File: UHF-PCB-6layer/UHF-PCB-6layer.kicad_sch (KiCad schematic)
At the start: 34 parts, among them IC1 MC100EL1648DG, J1 Screw_Terminal_01x07, J2 Screw_Terminal_01x04, U1 MAC-24+, U2 LTC1566-1IS8-PBF, U3 TAV1-331+, U4 MAC-24+, U5 XMSM0G3507SPT, U6 XC7A100T-CSG324_A

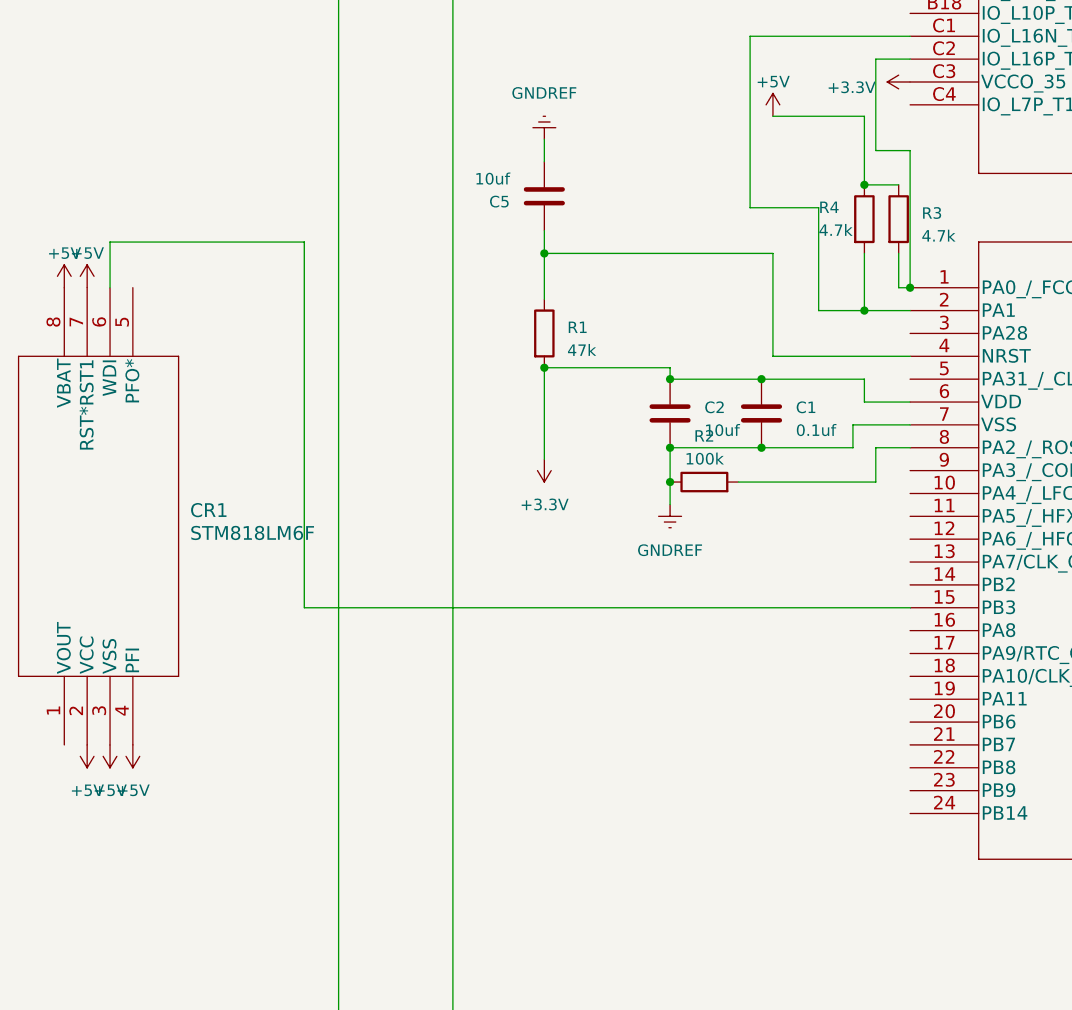
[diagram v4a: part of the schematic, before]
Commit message: draft of SVC added, needs to be vetted
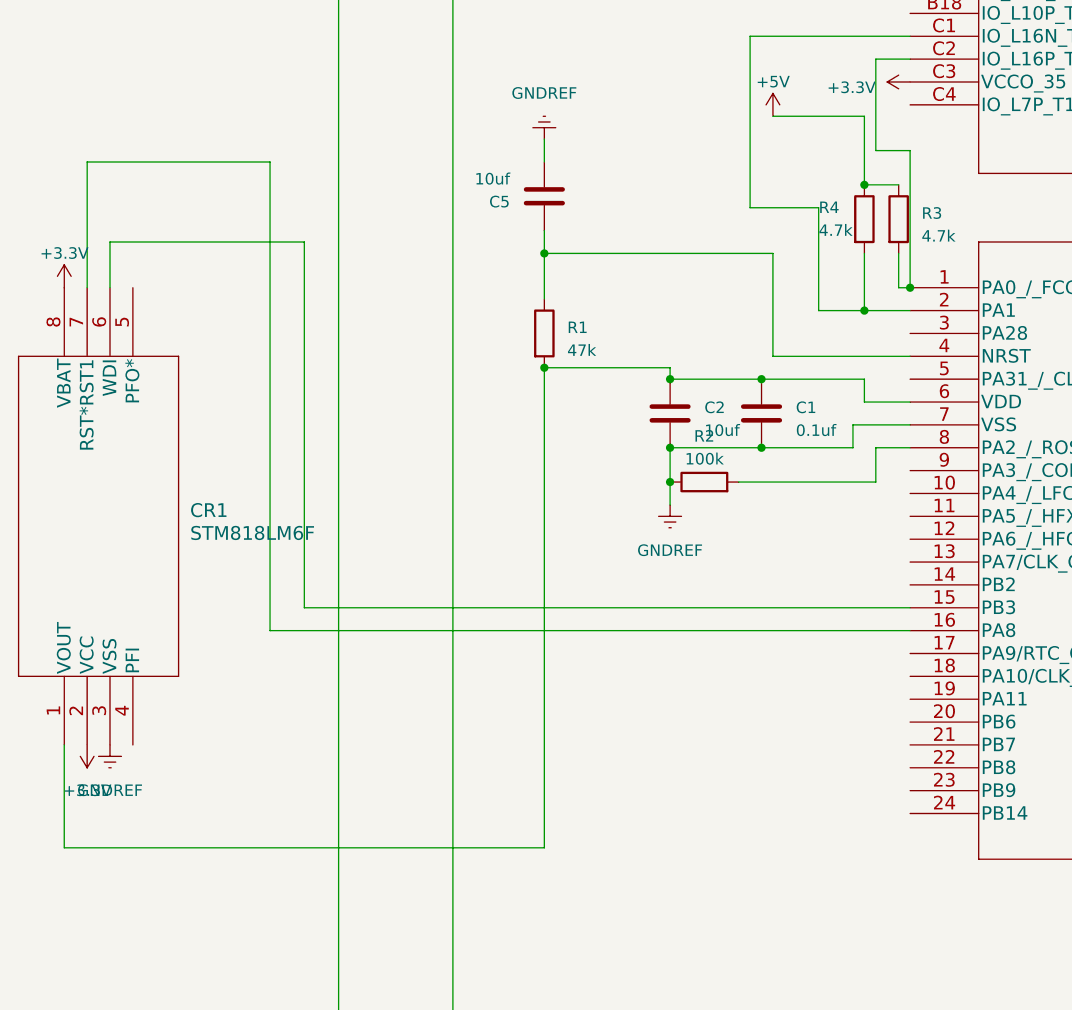
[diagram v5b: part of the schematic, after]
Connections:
- net +3.3V: now also CR1.2 (VCC), CR1.8 (VBAT); no longer C1.2, C2.2, R1.2, U5.6 (VDD)
- net +5V: no longer CR1.2 (VCC), CR1.3 (VSS), CR1.4 (PFI), CR1.7 (RST*RST1), CR1.8 (VBAT)
- net GNDREF: now also CR1.3 (VSS)
- net at CR1.1 (VOUT): now also C1.2, C2.2, R1.2, U5.6 (VDD)
- net at U5.16 (PA8): now also CR1.7 (RST*RST1)
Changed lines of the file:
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@@
+    (stroke (width 0) (type default))
+  )
+  (wire (pts (xy 57.15 209.55) (xy 128.27 209.55))
     (stroke (width 0) (type default))
   )
@@
     (stroke (width 0) (type default))
   )
+  (wire (pts (xy 87.63 233.68) (xy 34.29 233.68))
+    (stroke (width 0) (type default))
+  )
   (wire (pts (xy 295.91 222.25) (xy 290.83 222.25))
     (stroke (width 0) (type default))
@@
     (stroke (width 0) (type default))
   )
+  (wire (pts (xy 57.15 157.48) (xy 57.15 209.55))
+    (stroke (width 0) (type default))
+  )
+  (wire (pts (xy 36.83 171.45) (xy 36.83 157.48))
+    (stroke (width 0) (type default))
+  )
   (wire (pts (xy 267.97 190.5) (xy 267.97 194.31))
     (stroke (width 0) (type default))
@@
     (stroke (width 0) (type default))
   )
+  (wire (pts (xy 36.83 157.48) (xy 57.15 157.48))
+    (stroke (width 0) (type default))
+  )
   (wire (pts (xy 269.24 173.99) (xy 287.02 173.99))
     (stroke (width 0) (type default))
@@
     (stroke (width 0) (type default))
   )
-  (wire (pts (xy 87.63 180.34) (xy 87.63 190.5))
+  (wire (pts (xy 87.63 180.34) (xy 87.63 233.68))
     (stroke (width 0) (type default))
   )
@@
     (stroke (width 0) (type default))
   )
+  (wire (pts (xy 34.29 233.68) (xy 34.29 222.25))
+    (stroke (width 0) (type default))
+  )
   (wire (pts (xy 431.8 256.54) (xy 431.8 153.67))
     (stroke (width 0) (type default))
@@
     (stroke (width 0) (type default))
   )
+  (symbol (lib_id "power:+3.3V") (at 36.83 222.25 180) (unit 1)
+    (in_bom yes) (on_board yes) (dnp no) (fields_autoplaced)
+    (property "Reference" "#PWR044" (at 36.83 218.44 0)
+      (effects (font (size 1.27 1.27)) hide)
+    )
+    (property "Value" "+3.3V" (at 36.83 227.33 0)
+      (effects (font (size 1.27 1.27)))
+    )
+    (property "Footprint" "" (at 36.83 222.25 0)
+      (effects (font (size 1.27 1.27)) hide)
+    )
+    (property "Datasheet" "" (at 36.83 222.25 0)
+      (effects (font (size 1.27 1.27)) hide)
+    )
+    (pin "1")
+    (instances
+      (project "UHF-PCB-6layer"
+        (path "/408f5dbf-8c57-4b84-b0cc-1d788fcf6d08"
+          (reference "#PWR044") (unit 1)
+        )
+      )
+    )
+  )
   (symbol (lib_id "Device:L") (at 290.83 173.99 90) (unit 1)
     (in_bom yes) (on_board yes) (dnp no) (fields_autoplaced)
@@
         (path "/408f5dbf-8c57-4b84-b0cc-1d788fcf6d08"
           (reference "L1") (unit 1)
-        )
-      )
-    )
-  )
-  (symbol (lib_id "power:+5V") (at 34.29 171.45 0) (unit 1)
-    (in_bom yes) (on_board yes) (dnp no) (fields_autoplaced)
-    (property "Reference" "#PWR045" (at 34.29 175.26 0)
-      (effects (font (size 1.27 1.27)) hide)
-    )
-    (property "Value" "+5V" (at 34.29 167.64 0)
-      (effects (font (size 1.27 1.27)))
-    )
-    (property "Footprint" "" (at 34.29 171.45 0)
-      (effects (font (size 1.27 1.27)) hide)
-    )
-    (property "Datasheet" "" (at 34.29 171.45 0)
-      (effects (font (size 1.27 1.27)) hide)
-    )
-    (pin "1")
-    (instances
-      (project "UHF-PCB-6layer"
-        (path "/408f5dbf-8c57-4b84-b0cc-1d788fcf6d08"
-          (reference "#PWR045") (unit 1)
         )
       )
@@
     )
   )
-  (symbol (lib_id "power:+5V") (at 36.83 222.25 180) (unit 1)
-    (in_bom yes) (on_board yes) (dnp no) (fields_autoplaced)
-    (property "Reference" "#PWR043" (at 36.83 218.44 0)
-      (effects (font (size 1.27 1.27)) hide)
-    )
-    (property "Value" "+5V" (at 36.83 227.33 0)
-      (effects (font (size 1.27 1.27)))
-    )
-    (property "Footprint" "" (at 36.83 222.25 0)
-      (effects (font (size 1.27 1.27)) hide)
-    )
-    (property "Datasheet" "" (at 36.83 222.25 0)
+  (symbol (lib_id "power:+3.3V") (at 34.29 171.45 0) (unit 1)
+    (in_bom yes) (on_board yes) (dnp no) (fields_autoplaced)
+    (property "Reference" "#PWR043" (at 34.29 175.26 0)
+      (effects (font (size 1.27 1.27)) hide)
+    )
+    (property "Value" "+3.3V" (at 34.29 167.64 0)
+      (effects (font (size 1.27 1.27)))
+    )
+    (property "Footprint" "" (at 34.29 171.45 0)
+      (effects (font (size 1.27 1.27)) hide)
+    )
+    (property "Datasheet" "" (at 34.29 171.45 0)
       (effects (font (size 1.27 1.27)) hide)
     )
@@
         (path "/408f5dbf-8c57-4b84-b0cc-1d788fcf6d08"
           (reference "#PWR035") (unit 1)
-        )
-      )
-    )
-  )
-  (symbol (lib_id "power:+5V") (at 39.37 222.25 180) (unit 1)
-    (in_bom yes) (on_board yes) (dnp no) (fields_autoplaced)
-    (property "Reference" "#PWR044" (at 39.37 218.44 0)
-      (effects (font (size 1.27 1.27)) hide)
-    )
-    (property "Value" "+5V" (at 39.37 227.33 0)
-      (effects (font (size 1.27 1.27)))
-    )
-    (property "Footprint" "" (at 39.37 222.25 0)
-      (effects (font (size 1.27 1.27)) hide)
-    )
-    (property "Datasheet" "" (at 39.37 222.25 0)
-      (effects (font (size 1.27 1.27)) hide)
-    )
-    (pin "1")
-    (instances
-      (project "UHF-PCB-6layer"
-        (path "/408f5dbf-8c57-4b84-b0cc-1d788fcf6d08"
-          (reference "#PWR044") (unit 1)
         )
       )
@@
         (path "/408f5dbf-8c57-4b84-b0cc-1d788fcf6d08"
           (reference "U5") (unit 1)
-        )
-      )
-    )
-  )
-  (symbol (lib_id "power:+3.3V") (at 87.63 190.5 180) (unit 1)
-    (in_bom yes) (on_board yes) (dnp no) (fields_autoplaced)
-    (property "Reference" "#PWR04" (at 87.63 186.69 0)
-      (effects (font (size 1.27 1.27)) hide)
-    )
-    (property "Value" "+3.3V" (at 87.63 195.58 0)
-      (effects (font (size 1.27 1.27)))
-    )
-    (property "Footprint" "" (at 87.63 190.5 0)
-      (effects (font (size 1.27 1.27)) hide)
-    )
-    (property "Datasheet" "" (at 87.63 190.5 0)
-      (effects (font (size 1.27 1.27)) hide)
-    )
-    (pin "1")
-    (instances
-      (project "UHF-PCB-6layer"
-        (path "/408f5dbf-8c57-4b84-b0cc-1d788fcf6d08"
-          (reference "#PWR04") (unit 1)
         )
       )
@@
     )
   )
+  (symbol (lib_id "power:GNDREF") (at 39.37 222.25 0) (unit 1)
+    (in_bom yes) (on_board yes) (dnp no) (fields_autoplaced)
+    (property "Reference" "#PWR045" (at 39.37 228.6 0)
+      (effects (font (size 1.27 1.27)) hide)
+    )
+    (property "Value" "GNDREF" (at 39.37 227.33 0)
+      (effects (font (size 1.27 1.27)))
+    )
+    (property "Footprint" "" (at 39.37 222.25 0)
+      (effects (font (size 1.27 1.27)) hide)
+    )
+    (property "Datasheet" "" (at 39.37 222.25 0)
+      (effects (font (size 1.27 1.27)) hide)
+    )
+    (pin "1")
+    (instances
+      (project "UHF-PCB-6layer"
+        (path "/408f5dbf-8c57-4b84-b0cc-1d788fcf6d08"
+          (reference "#PWR045") (unit 1)
+        )
+      )
+    )
+  )
   (symbol (lib_id "Device:LED") (at 326.39 27.94 0) (unit 1)
     (in_bom yes) (on_board yes) (dnp no) (fields_autoplaced)
@@
         (path "/408f5dbf-8c57-4b84-b0cc-1d788fcf6d08"
           (reference "#PWR012") (unit 1)
-        )
-      )
-    )
-  )
-  (symbol (lib_id "power:+5V") (at 41.91 222.25 180) (unit 1)
-    (in_bom yes) (on_board yes) (dnp no) (fields_autoplaced)
-    (property "Reference" "#PWR046" (at 41.91 218.44 0)
-      (effects (font (size 1.27 1.27)) hide)
-    )
-    (property "Value" "+5V" (at 41.91 227.33 0)
-      (effects (font (size 1.27 1.27)))
-    )
-    (property "Footprint" "" (at 41.91 222.25 0)
-      (effects (font (size 1.27 1.27)) hide)
-    )
-    (property "Datasheet" "" (at 41.91 222.25 0)
-      (effects (font (size 1.27 1.27)) hide)
-    )
-    (pin "1")
-    (instances
-      (project "UHF-PCB-6layer"
-        (path "/408f5dbf-8c57-4b84-b0cc-1d788fcf6d08"
-          (reference "#PWR046") (unit 1)
         )
       )
@@
         )
       )
-    )
-  )
-  (symbol (lib_id "power:+5V") (at 36.83 171.45 0) (unit 1)
-    (in_bom yes) (on_board yes) (dnp no) (fields_autoplaced)
-    (property "Reference" "#PWR047" (at 36.83 175.26 0)
-      (effects (font (size 1.27 1.27)) hide)
-    )
-    (property "Value" "+5V" (at 36.83 167.64 0)
-      (effects (font (size 1.27 1.27)))
-    )
-    (property "Footprint" "" (at 36.83 171.45 0)
-      (effects (font (size 1.27 1.27)) hide)
-    )
-    (property "Datasheet" "" (at 36.83 171.45 0)
-      (effects (font (size 1.27 1.27)) hide)
-    )
-    (pin "1")
-    (instances
-      (project "UHF-PCB-6layer"
-        (path "/408f5dbf-8c57-4b84-b0cc-1d788fcf6d08"
-          (reference "#PWR047") (unit 1)
-        )
-      )

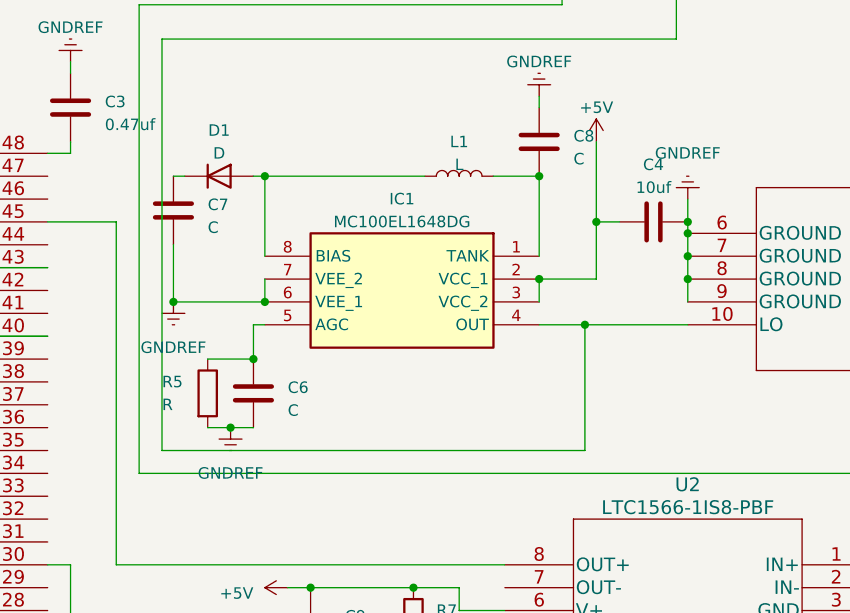
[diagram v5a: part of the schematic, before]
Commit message: added new mixer to schematic
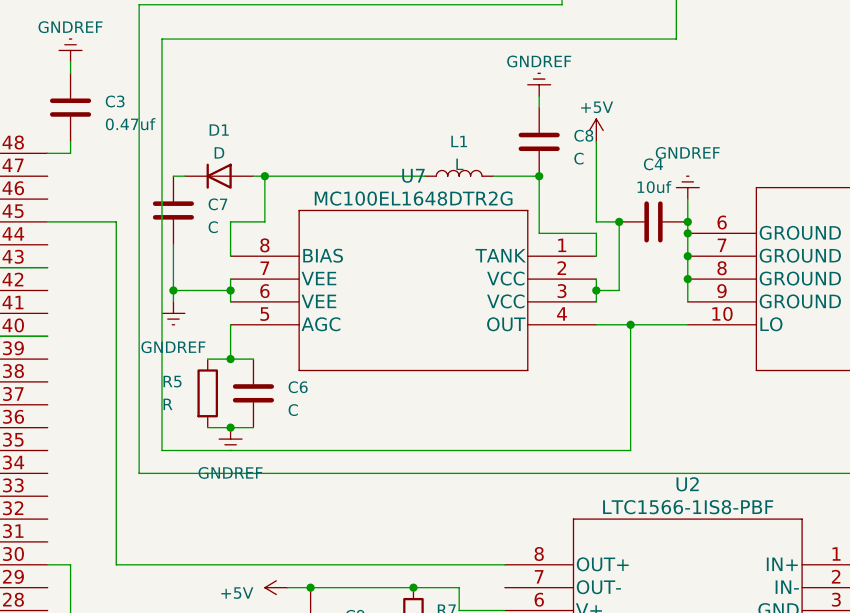
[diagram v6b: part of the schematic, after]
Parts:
- removed IC1: MC100EL1648DG, SOIC127P600X175-8N, symbol MC100EL1648DG:MC100EL1648DG
- added U7: MC100EL1648DTR2G, TSSOP8_3P10X3P10_ONS, symbol VCO2:MC100EL1648DTR2G
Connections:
- net +5V: now also U7.2 (VCC), U7.3 (VCC)
- net GNDREF: now also U7.6 (VEE), U7.7 (VEE)
- net at D1.2 (A), L1.1: now also U7.8 (BIAS)
- net at C8.1, L1.2: now also U7.1 (TANK)
- net at U1.10 (LO), U4.10 (LO): now also U7.4 (OUT)
- net at C6.2, R5.1: now also U7.5 (AGC)

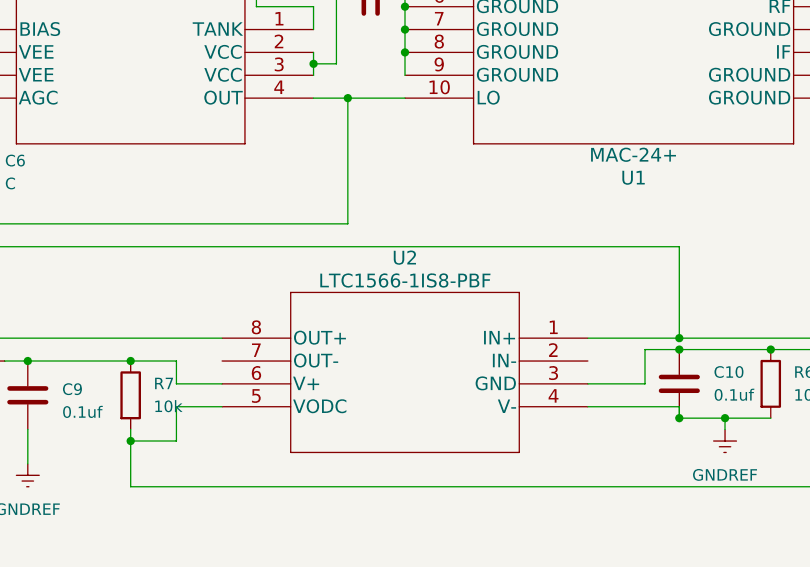
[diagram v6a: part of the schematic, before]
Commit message: added footprints to all schematic symbols and added to pcb
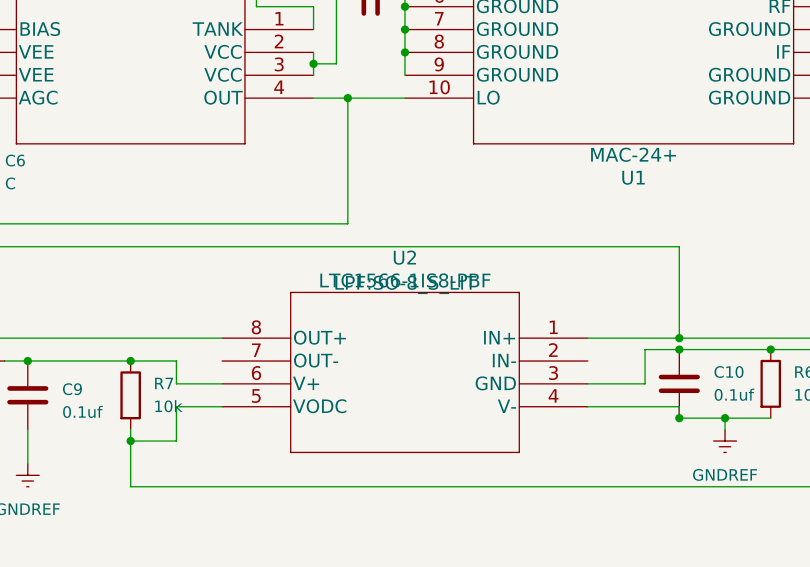
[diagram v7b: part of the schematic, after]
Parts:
- CR1: footprint SO-8_STM -> WDT:SO-8_STM
- FL1: footprint HF1139_MNC -> BPF:HF1139_MNC
- J2: footprint TerminalBlock:TerminalBlock_bornier-4_P5.08mm -> TerminalBlock_Altech:Altech_AK300_1x07_P5.00mm_45-Degree
- U1, U4: footprint DZ1650_MNC -> MIX:DZ1650_MNC
- U2: footprint SO-8_S_LIT -> LPF:SO-8_S_LIT
- U3: footprint TE2769_MNC -> LNA:TE2769_MNC
- U5: footprint LQFP48_PT_TEX -> MC:LQFP48_PT_TEX
- U6: footprint CS/CSG324_XIL -> fpga:CS&slash_CSG324_XIL
- U7: footprint TSSOP8_3P10X3P10_ONS -> VCO:TSSOP8_3P10X3P10_ONS
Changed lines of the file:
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@@
       (effects (font (size 1.524 1.524)) (justify right))
     )
-    (property "Footprint" "SO-8_STM" (at 28.194 196.85 0)
+    (property "Footprint" "WDT:SO-8_STM" (at 28.194 196.85 0)
       (effects (font (size 1.524 1.524)) hide)
     )
@@
       (effects (font (size 1.524 1.524)))
     )
-    (property "Footprint" "DZ1650_MNC" (at 341.63 196.596 0)
+    (property "Footprint" "MIX:DZ1650_MNC" (at 341.63 196.596 0)
       (effects (font (size 1.524 1.524)) hide)
     )
@@
       (effects (font (size 1.524 1.524)))
     )
-    (property "Footprint" "SO-8_S_LIT" (at 316.23 211.074 0)
-      (effects (font (size 1.524 1.524)) hide)
+    (property "Footprint" "LPF:SO-8_S_LIT" (at 316.23 211.074 0)
+      (effects (font (size 1.524 1.524)))
     )
     (property "Datasheet" "" (at 336.55 217.17 0)
@@
       (effects (font (size 1.524 1.524)))
     )
-    (property "Footprint" "TE2769_MNC" (at 367.284 157.48 0)
+    (property "Footprint" "LNA:TE2769_MNC" (at 367.284 157.48 0)
       (effects (font (size 1.524 1.524)) hide)
     )
@@
       (effects (font (size 1.524 1.524)))
     )
-    (property "Footprint" "HF1139_MNC" (at 417.83 115.824 0)
+    (property "Footprint" "BPF:HF1139_MNC" (at 417.83 115.824 0)
       (effects (font (size 1.524 1.524)) hide)
     )
@@
       (effects (font (size 1.524 1.524)))
     )
-    (property "Footprint" "DZ1650_MNC" (at 416.56 92.964 0)
+    (property "Footprint" "MIX:DZ1650_MNC" (at 416.56 92.964 0)
       (effects (font (size 1.524 1.524)) hide)
     )
@@
       (effects (font (size 1.524 1.524)))
     )
-    (property "Footprint" "LQFP48_PT_TEX" (at 186.69 165.354 0)
+    (property "Footprint" "MC:LQFP48_PT_TEX" (at 186.69 165.354 0)
       (effects (font (size 1.524 1.524)) hide)
     )
@@
       (effects (font (size 1.524 1.524)))
     )
-    (property "Footprint" "CS/CSG324_XIL" (at 184.15 45.974 0)
+    (property "Footprint" "fpga:CS&slash_CSG324_XIL" (at 184.15 45.974 0)
       (effects (font (size 1.524 1.524)) hide)
     )
@@
       (effects (font (size 1.524 1.524)))
     )
-    (property "Footprint" "TSSOP8_3P10X3P10_ONS" (at 285.75 176.784 0)
+    (property "Footprint" "VCO:TSSOP8_3P10X3P10_ONS" (at 285.75 176.784 0)
       (effects (font (size 1.524 1.524)) hide)
     )
@@
       (effects (font (size 1.27 1.27)))
     )
-    (property "Footprint" "TerminalBlock:TerminalBlock_bornier-4_P5.08mm" (at 335.28 21.59 0)
-      (effects (font (size 1.27 1.27)) hide)
-    )
+    (property "Footprint" "TerminalBlock_Altech:Altech_AK300_1x07_P5.00mm_45-Degree" (at 335.28 21.59 0)
+      (effects (font (size 1.27 1.27)) hide)
+    )
